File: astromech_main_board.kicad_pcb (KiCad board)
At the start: 2 copper layers, 71.6 x 78 mm, 75 parts, among them IC1 MAX11645EUA+, J1 Conn_01x03, J10 61201621621, J11 Conn_01x06, J15 Conn_01x04, J18 Screw_Terminal_01x10, J19 Conn_01x04, J2 Conn_02x03_Odd_Even, J20 Conn_01x04, J21 Conn_01x04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

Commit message: somewhat routed
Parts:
- R20, R21: moved to B.Cu
- moved R21 15.9 mm to (175.5, 140.0), turned to 0 degrees
- moved R20 14.0 mm to (183.9, 139.7), turned to 180 degrees
- moved C7 13.2 mm to (197.2, 135.1)
- moved C8 13.2 mm to (197.2, 125.0)
- moved R12 13.2 mm to (197.2, 130.0)
- moved Y1 13.2 mm to (193.3, 130.0)
- moved C10 8.38 mm to (177.0, 126.0), turned to -90 degrees
- moved C12 3.56 mm to (177.0, 110.2)
- moved R3 3.44 mm to (192.3, 123.7), turned to -90 degrees
- moved R6 3.30 mm to (193.2, 112.5)
- moved R5 2.54 mm to (193.2, 109.2)
- moved C11 2.50 mm to (177.0, 118.1)
- turned R13 to 0 degrees
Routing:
- net /I2C_3V3_SCL: track 6.39 -> 140.9 mm, vias 0 -> 8
- net /I2C_3V3_SDA: track 7.65 -> 141.0 mm, vias 0 -> 6
- net /PWM_RIGHT: track 0.00 -> 116.4 mm
- net /IOTX: track 0.00 -> 103.5 mm
- net /PWM_LEFT: track 0.00 -> 102.4 mm, vias 0 -> 2
- net /IORX: track 0.00 -> 102.2 mm, vias 0 -> 2
- net /ENC_INT: track 0.00 -> 64.9 mm
- net /IO45: track 0.00 -> 64.8 mm, vias 0 -> 1
- net Net-(U10-FCKI): track 0.00 -> 57.7 mm, vias 0 -> 2
- net /HEAD_B: track 0.00 -> 51.5 mm
- net /RIGHT_B: track 0.00 -> 48.4 mm
- net /LEFT_B: track 0.00 -> 48.0 mm
- net /HEAD_A: track 0.00 -> 47.6 mm
- net /IO40: track 0.00 -> 47.1 mm, vias 0 -> 1
- net /IO8: track 0.00 -> 46.3 mm
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
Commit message: 3v3 routed
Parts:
- moved R4 6.48 mm to (217.2, 106.2)
- moved R16 5.46 mm to (217.2, 99.3)
- moved Q1 1.45 mm to (203.7, 107.3)
- moved C10 0.51 mm to (177.0, 125.5)
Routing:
- net 5V: track 44.6 -> 135.1 mm, vias 0 -> 6
- net 3V3: track 26.2 -> 88.1 mm, vias 8 -> 30
- net Net-(U9-FCKO): track 8.98 -> 59.3 mm, vias 0 -> 1
- net /IO4: track 0.00 -> 49.1 mm, vias 0 -> 2
- net /TOUCH_X+: track 0.00 -> 44.3 mm, vias 0 -> 6
- net /TOUCH_Y+: track 0.00 -> 40.1 mm, vias 0 -> 1
- net /IO18: track 0.00 -> 35.7 mm, vias 0 -> 2
- net /IO3: track 0.00 -> 34.7 mm, vias 0 -> 6
- net /RST: track 0.00 -> 34.3 mm, vias 0 -> 4
- net /IO1: track 0.00 -> 26.9 mm, vias 0 -> 3
- net /IO2: track 0.00 -> 19.7 mm
- net /IO39: track 0.00 -> 14.9 mm
- net /RC_UART_5V: track 0.00 -> 14.4 mm, vias 0 -> 1
- net /SCR_D/C: track 0.00 -> 12.8 mm
- net /TOUCH_X-: track 0.00 -> 12.7 mm
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- added copper zone on F.Cu, net 3V3
- added copper zone on F.Cu, net 5V

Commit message: finished routing
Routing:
- net GND: track 0.00 -> 113.2 mm, vias 0 -> 36
- net /UART_RXA: track 35.6 -> 31.9 mm, vias 2 -> 4
- net Net-(D2-K): track 44.7 -> 43.4 mm
- net Net-(J4-Pin_3): track 26.1 -> 24.8 mm
- net Net-(J4-Pin_4): track 24.2 -> 22.9 mm
- net Net-(D1-K): track 38.1 -> 36.8 mm
- net 3V3: track 88.1 -> 89.2 mm
- net /LEFT_B: track 47.0 -> 48.0 mm
- net Net-(J4-Pin_5): track 22.3 -> 21.5 mm
- net 5V: track 135.1 -> 134.3 mm, vias 6 -> 5
- net /PWM_HEAD: track 42.5 -> 43.1 mm
- net /PWM_RIGHT: track 119.1 -> 119.6 mm
- added copper zone on B.Cu, net GND

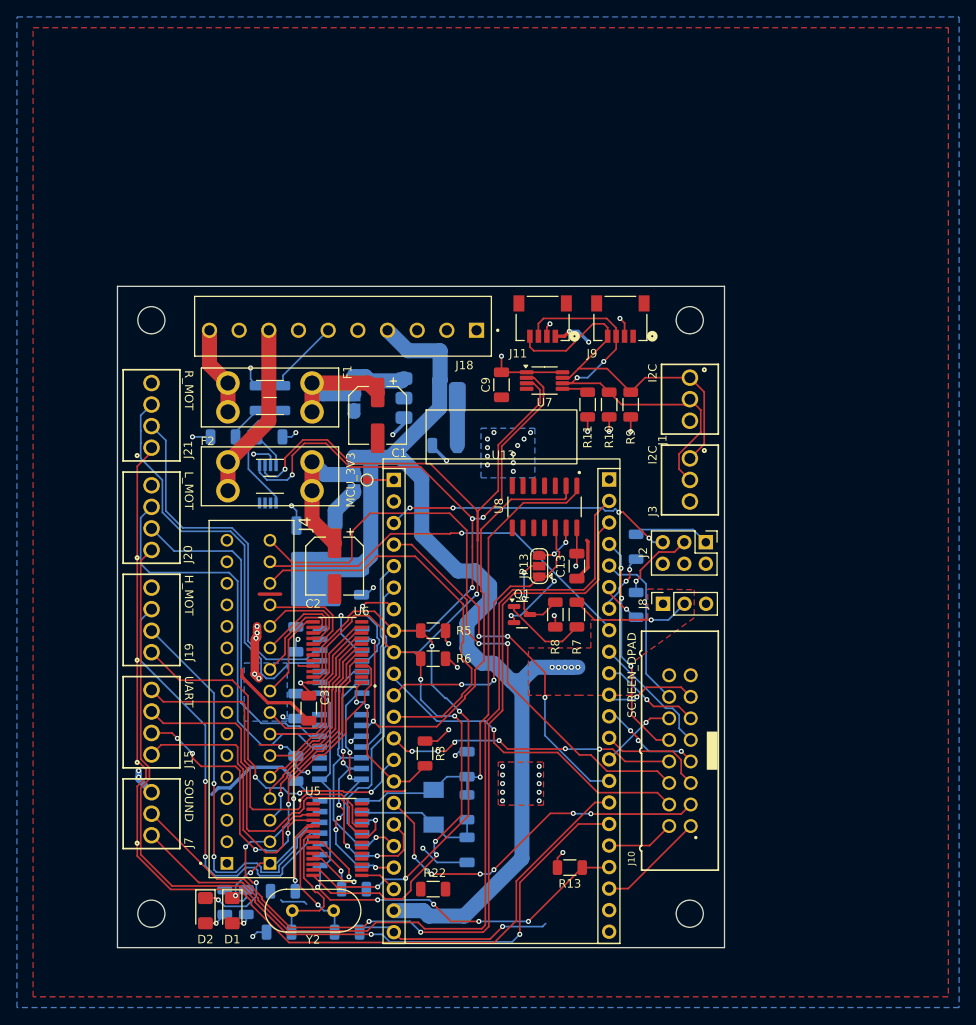
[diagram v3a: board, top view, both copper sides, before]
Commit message: switched motor terminal positions, adjusted silkscreen and routing
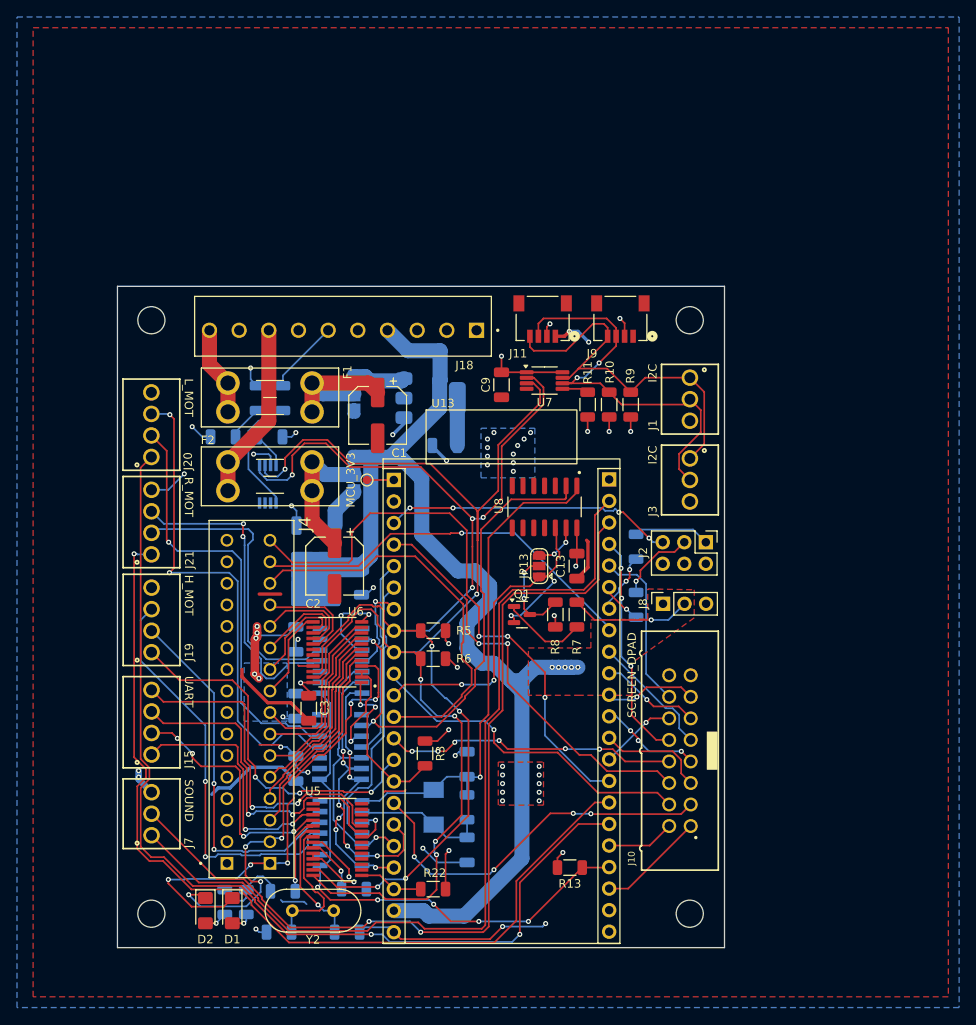
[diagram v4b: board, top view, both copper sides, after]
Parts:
- moved J21 12.6 mm to (160.0, 96.4)
- moved J20 11.0 mm to (160.0, 84.9)
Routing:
- net GND: track 113.2 -> 132.7 mm, vias 36 -> 39
- net Net-(D1-K): track 36.8 -> 56.0 mm, vias 3 -> 5
- net 3V3: track 89.2 -> 103.9 mm, vias 30 -> 31
- net /PWM_RIGHT: track 119.6 -> 108.0 mm, vias 0 -> 1
- net /RIGHT_B: track 49.6 -> 38.1 mm, vias 0 -> 2
- net /LEFT_A: track 39.9 -> 50.6 mm, vias 0 -> 1
- net /PWM_LEFT: track 106.3 -> 116.7 mm
- net /LEFT_B: track 48.0 -> 58.2 mm, vias 0 -> 2
- net /RIGHT_A: track 43.3 -> 35.5 mm
- net /HEAD_A: track 48.6 -> 42.9 mm
- net Net-(D2-K): track 43.4 -> 49.0 mm
- net /UART_TXA: track 33.3 -> 29.5 mm, vias 0 -> 2
- net /HEAD_B: track 51.9 -> 48.4 mm
- net /IO14: track 4.46 -> 7.63 mm
- net /I2C_3V3_SDA: track 144.2 -> 147.1 mm
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
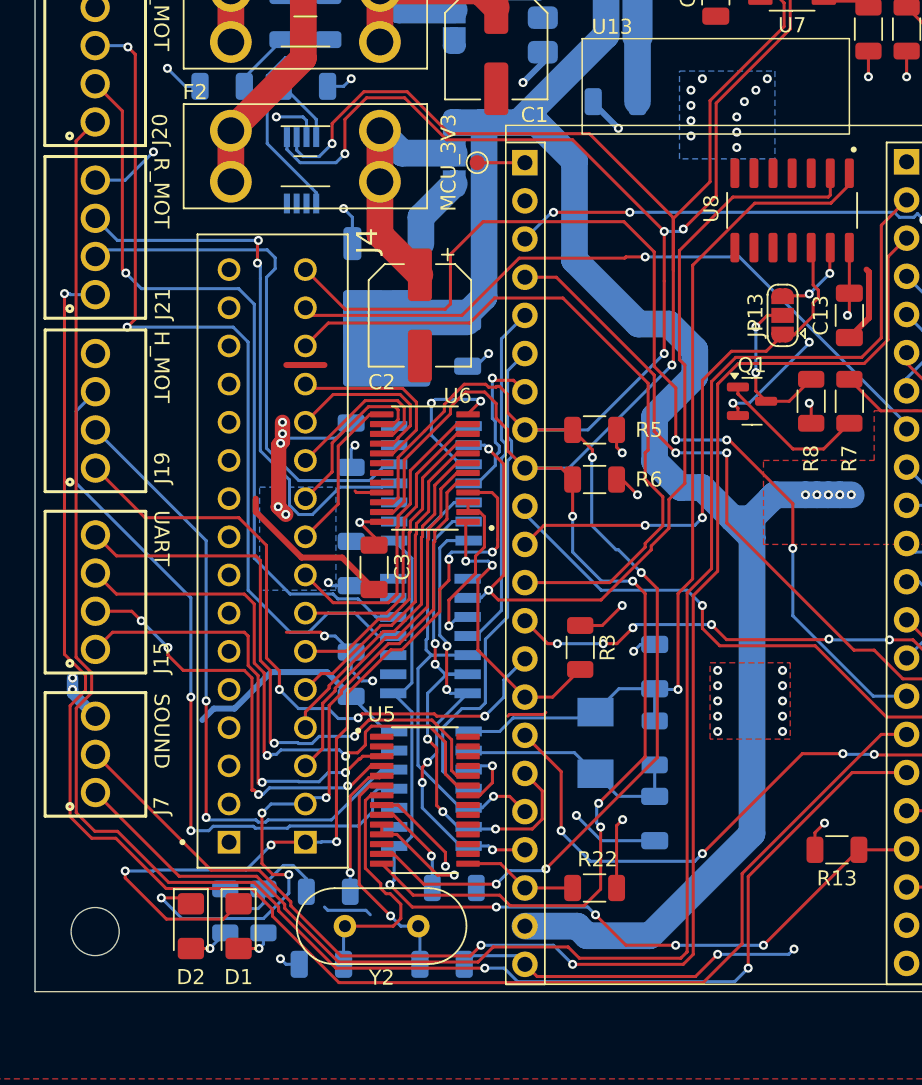
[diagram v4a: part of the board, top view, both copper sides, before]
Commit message: reordered terminal blocks
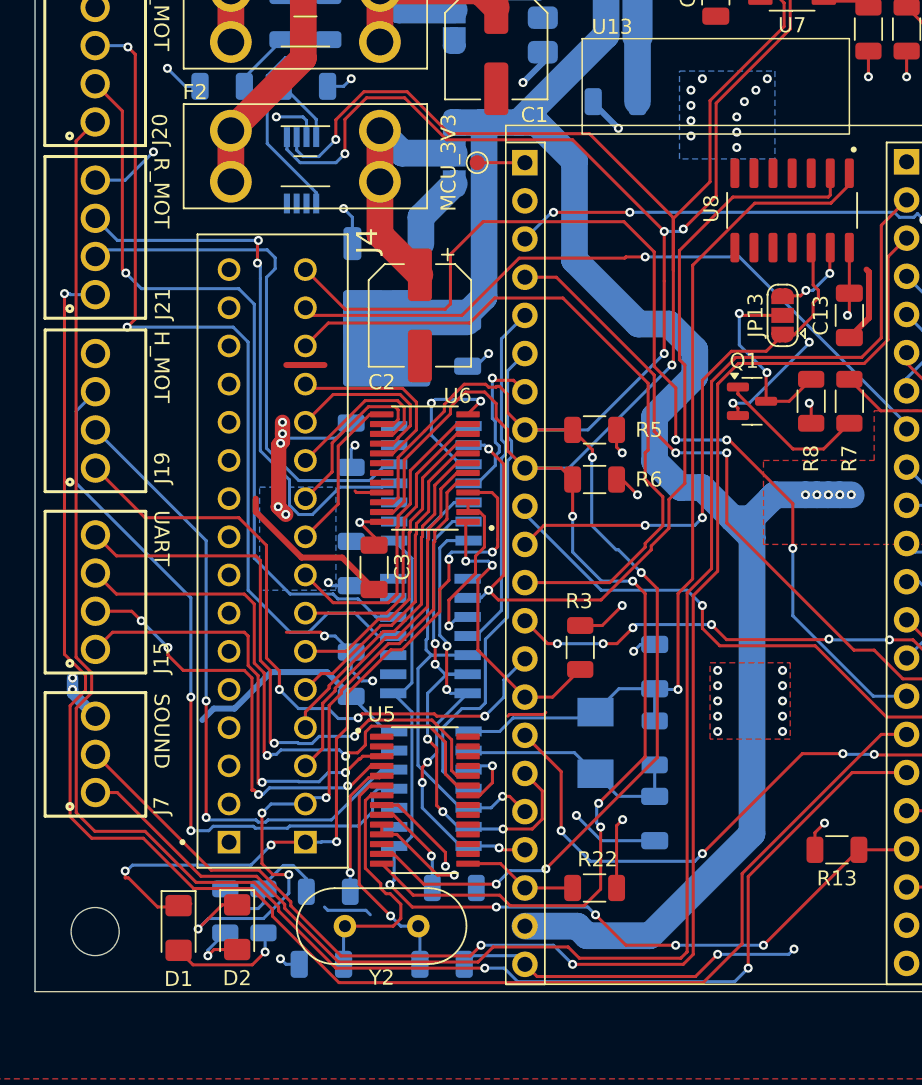
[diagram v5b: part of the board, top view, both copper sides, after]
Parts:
- moved D1 4.00 mm to (165.6, 142.4)
- moved D2 3.08 mm to (169.4, 142.3)
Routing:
- net Net-(D1-A): track 2.52 -> 7.83 mm
- net Net-(D1-K): track 56.0 -> 51.8 mm
- net Net-(JP13-C): track 10.9 -> 13.2 mm
- net Net-(D2-K): track 49.0 -> 47.4 mm
- net Net-(D2-A): track 2.73 -> 4.12 mm

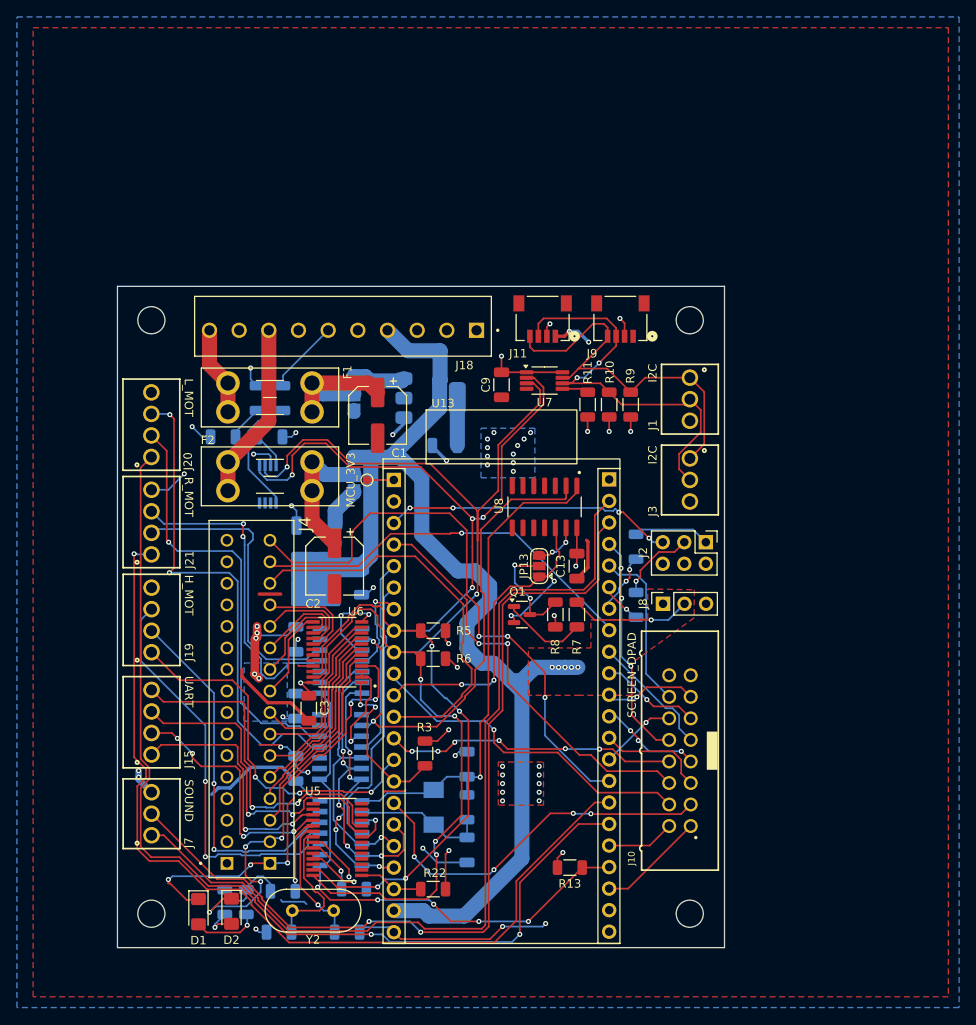
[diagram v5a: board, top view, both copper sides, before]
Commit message: added silkscreen
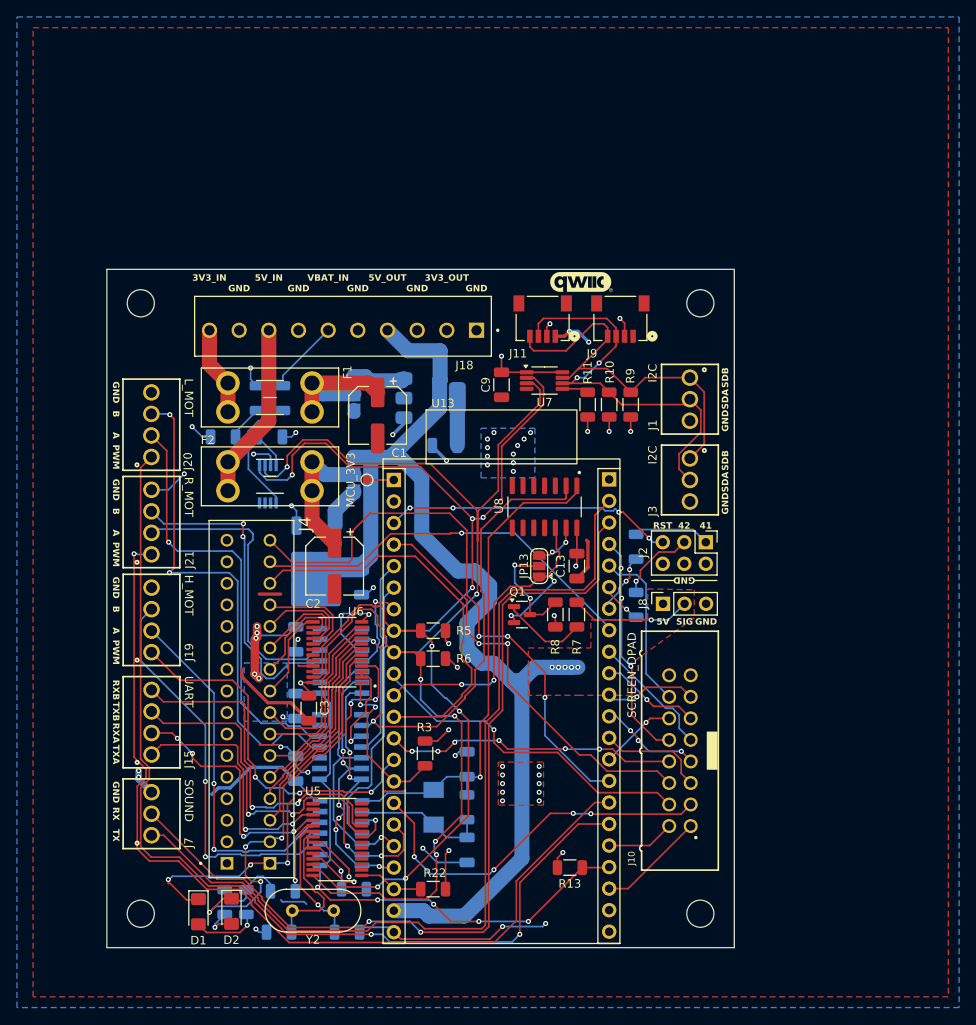
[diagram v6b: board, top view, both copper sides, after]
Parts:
- added G***: LOGO, LOGO, F.Cu at (210.7, 68.0)
- added G***: LOGO, LOGO, B.Cu at (211.8, 80.6)
- moved H1 2.36 mm to (158.8, 70.6)
- moved H2 2.36 mm to (224.8, 70.6)
- moved H3 1.25 mm to (158.8, 142.6)
- moved H4 1.25 mm to (224.8, 142.6)
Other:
- board size 71.6 x 78 mm -> 74 x 80 mm
- board text added: "3V3"
- board text added: "3V3_IN"
- board text added: "3V3_OUT"
- board text added: "41"
- board text added: "42"
- board text added: "5V"
- board text added: "5V_IN"
- board text added: "5V_OUT"
- board text added: "A"
- board text added: "Astromech Main Board Capstone 2025 Team {dblquote}Naboo Networks{dblquote} Rev1"
- board text added: "B"
- board text added: "D/C"
- board text added: "DPAD_C"
- board text added: "DPAD_D"
- board text added: "DPAD_L"
- board text added: "DPAD_R"
- board text added: "DPAD_U"
- board text added: "IO40"
- board text added: "IO45"
- board text added: "IO8"
- board text added: "P00"
- board text added: "P01"
- board text added: "P02"
- board text added: "P03"
- board text added: "P04"
- board text added: "P05"
- board text added: "P06"
- board text added: "P07"
- board text added: "P10"
- board text added: "P11"
- board text added: "P12"
- board text added: "P13"
- board text added: "P14"
- board text added: "PWM"
- board text added: "RST"
- board text added: "RX"
- board text added: "RXA"
- board text added: "RXB"
- board text added: "SDA"
- board text added: "SDB"
- board text added: "SIG"
- board text added: "SPI"
- board text added: "TX"
- board text added: "TXA"
- board text added: "TXB"
- board text added: "VBAT_IN"
- board text added: "X+"
- board text added: "X-"
- board text added: "Y+"
- board text added: "Y-"

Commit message: fixed pinout and some silkscreen labels
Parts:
- renumbered D1 to LED1, D2 to LED2
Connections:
- J8 pad 1: 5V -> /RC_UART_5V
- J8 pad 2: /RC_UART_5V -> 5V
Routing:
- net /RC_UART_5V: track 14.4 -> 12.1 mm
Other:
- board text added: "SCL"
- board text removed: "SDB"
